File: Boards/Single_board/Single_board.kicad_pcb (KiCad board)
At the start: 2 copper layers, 169.9 x 190.9 mm, 116 parts, among them J1 POWER, J2 ICSP, J3 918-468K2029E50001, J4 918-468K2029E50001, J5 918-468K2029E50001, SW1 2V~12V SMD Mechanical Keyboar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, SW10 2V~12V SMD Mechanical Keyboar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, SW11 2V~12V SMD Mechanical Keyboar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, SW12 2V~12V SMD Mechanical Keyboar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, SW13 2V~12V SMD Mechanical Keyboar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, SW14 2V~12V SMD Mechanical Keyboar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, SW15 2V~12V SMD Mechanical Keyboar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, SW16 2V~12V SMD Mechanical Keyboar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, SW17 2V~12V SMD Mechanical Keyboar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, SW18 2V~12V SMD Mechanical Keyboar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, SW19 2V~12V SMD Mechanical Keyboar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, SW2 2V~12V SMD Mechanical Keyboar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, SW3 2V~12V SMD Mechanical Keyboar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, SW4 2V~12V SMD Mechanical Keyboar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, SW5 2V~12V SMD Mechanical Keyboar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, SW6 2V~12V SMD Mechanical Keyboar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, SW7 2V~12V SMD Mechanical Keyboar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, SW8 2V~12V SMD Mechanical Keyboar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, SW9 2V~12V SMD Mechanical Keyboar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, U2 ATmega328P-A, U3 CH340C

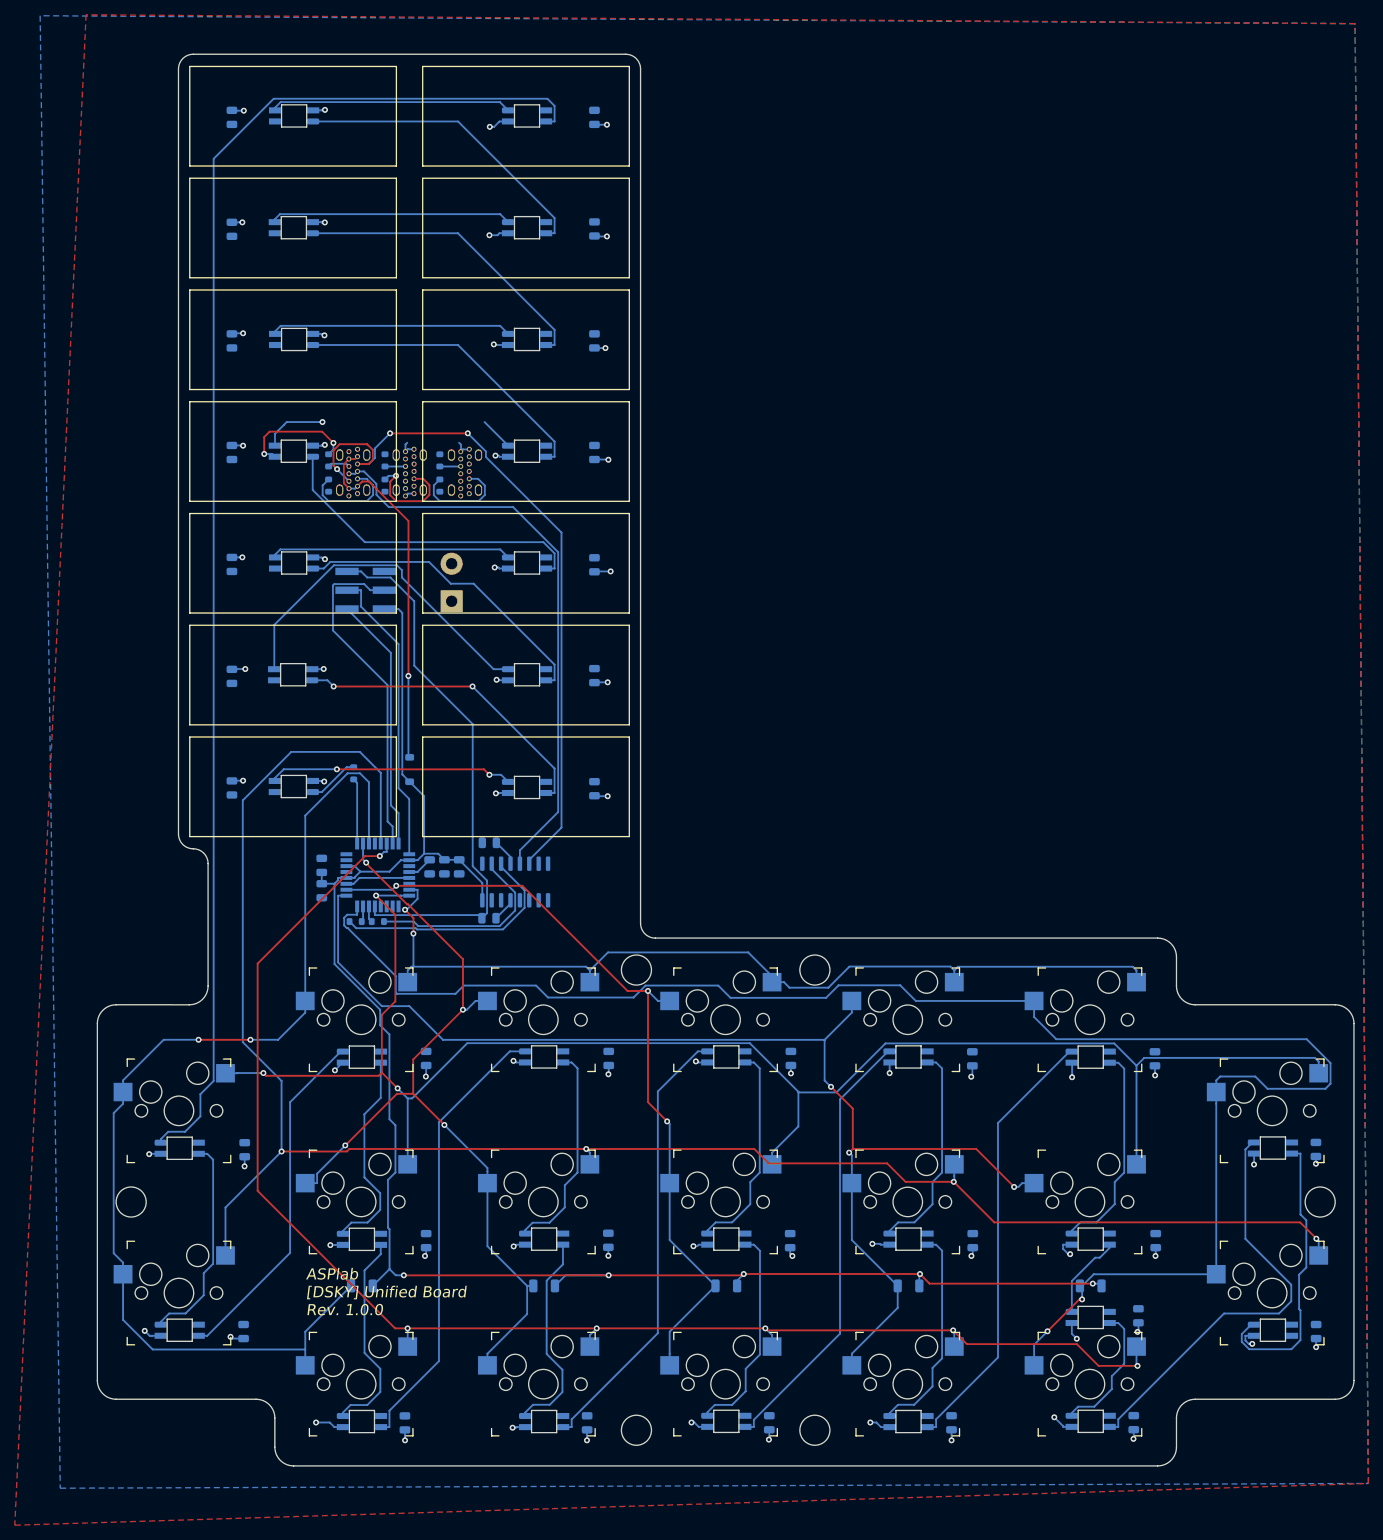
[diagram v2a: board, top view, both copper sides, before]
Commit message: Autoroute and change rgb led footprint
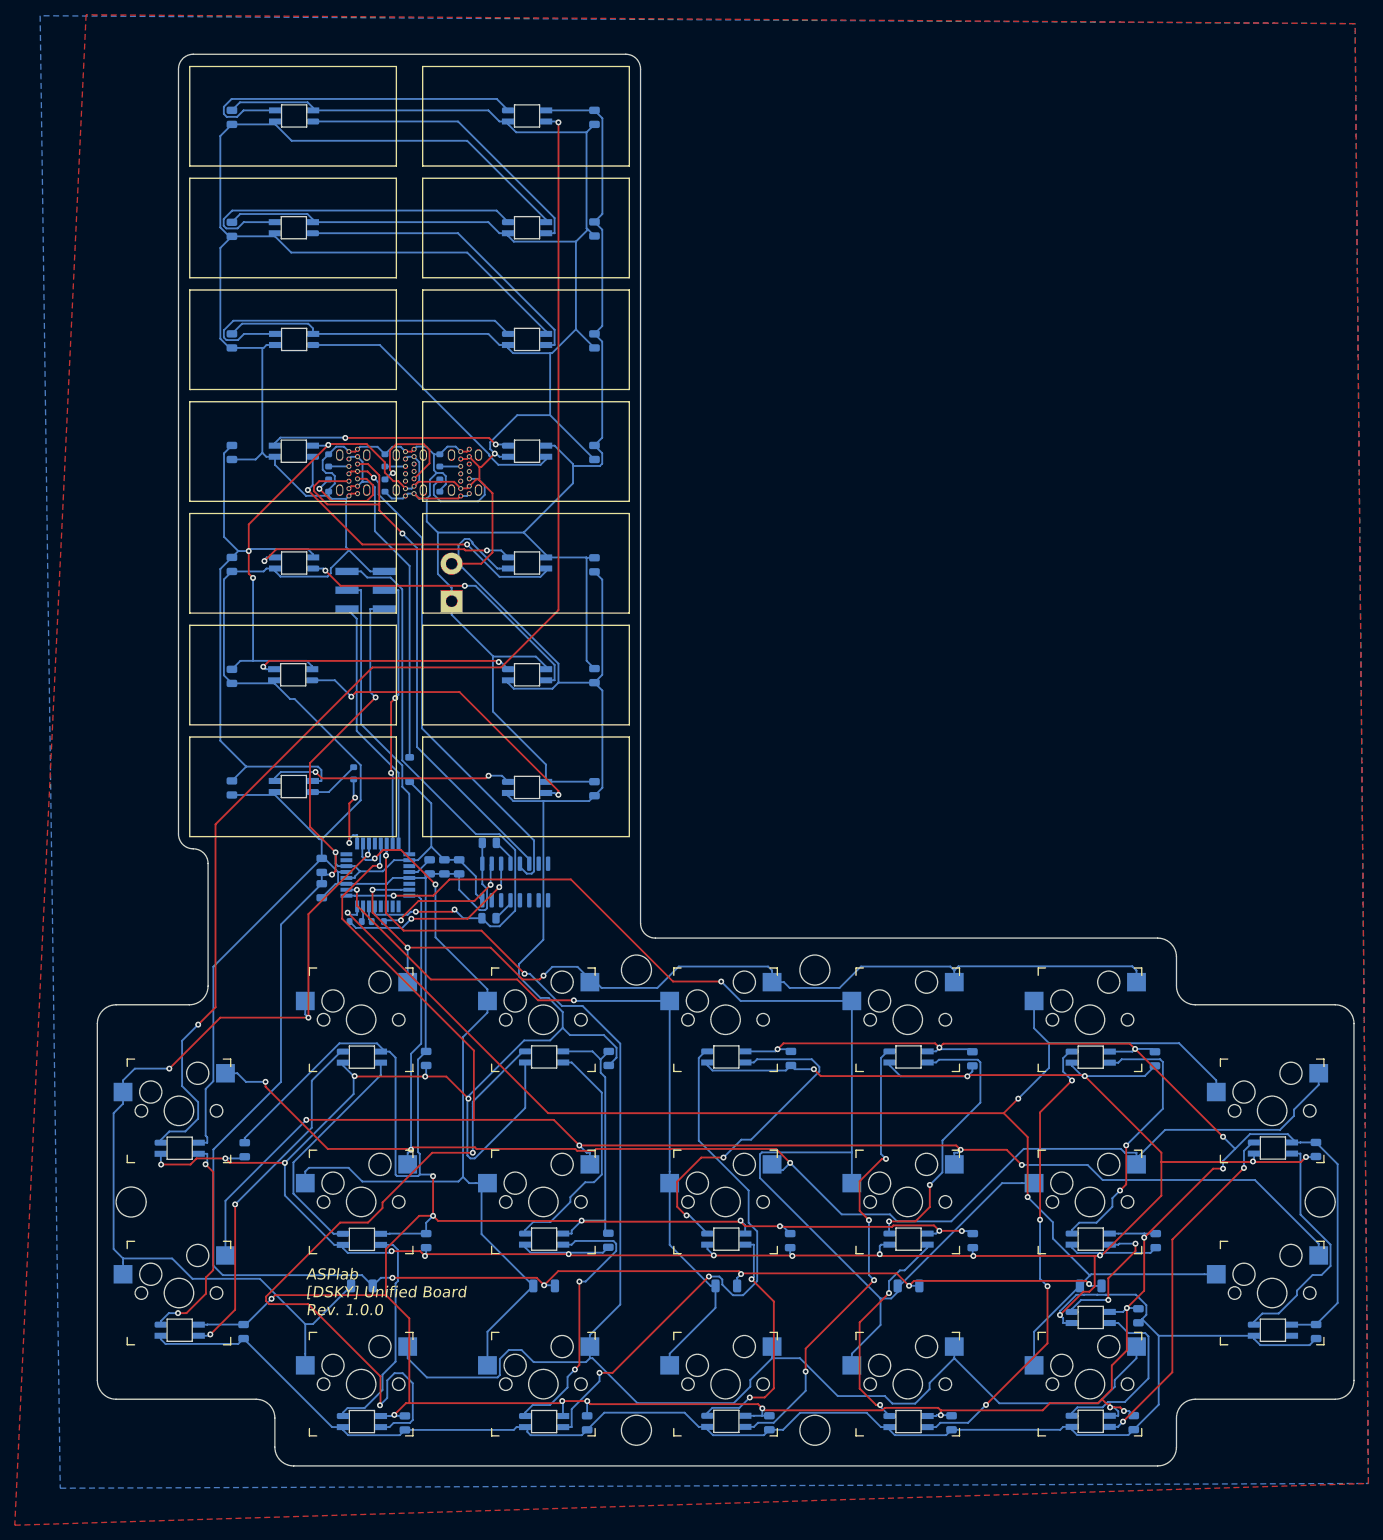
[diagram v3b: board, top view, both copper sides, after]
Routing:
- net GND: track 31.2 -> 1175.9 mm, vias 2 -> 22
- net 5V10A: track 119.2 -> 1129.4 mm, vias 68 -> 24
- net 5V1A: track 235.8 -> 273.0 mm, vias 5 -> 8
- net Net-(D19-DOUT): track 60.8 -> 95.4 mm, vias 0 -> 2
- net Y2: track 251.1 -> 221.7 mm, vias 4 -> 5
- net X4: track 229.8 -> 206.5 mm, vias 2 -> 3
- net Y3: track 197.5 -> 219.0 mm, vias 6 -> 2
- net X0: track 147.9 -> 127.4 mm, vias 2 -> 3
- net Net-(D7-DOUT): track 13.2 -> 32.7 mm, vias 1 -> 2
- net Net-(U3-UD-): track 97.3 -> 79.7 mm, vias 3 -> 1
- net Net-(D23-DOUT): track 28.9 -> 45.6 mm, vias 0 -> 2
- net Net-(D10-DIN): track 32.6 -> 48.1 mm
- net Net-(D13-DOUT): track 32.7 -> 48.0 mm
- net Net-(D11-DOUT): track 32.7 -> 47.9 mm
- net Net-(D14-DOUT): track 190.5 -> 175.3 mm, vias 0 -> 2
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- added copper zone on B.Cu, net 5V10A
- added copper zone on F.Cu, net GND
- removed copper zone on F.Cu, net 5V10A
- removed copper zone on B.Cu, net GND

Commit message: Fix led footprint & autoroute
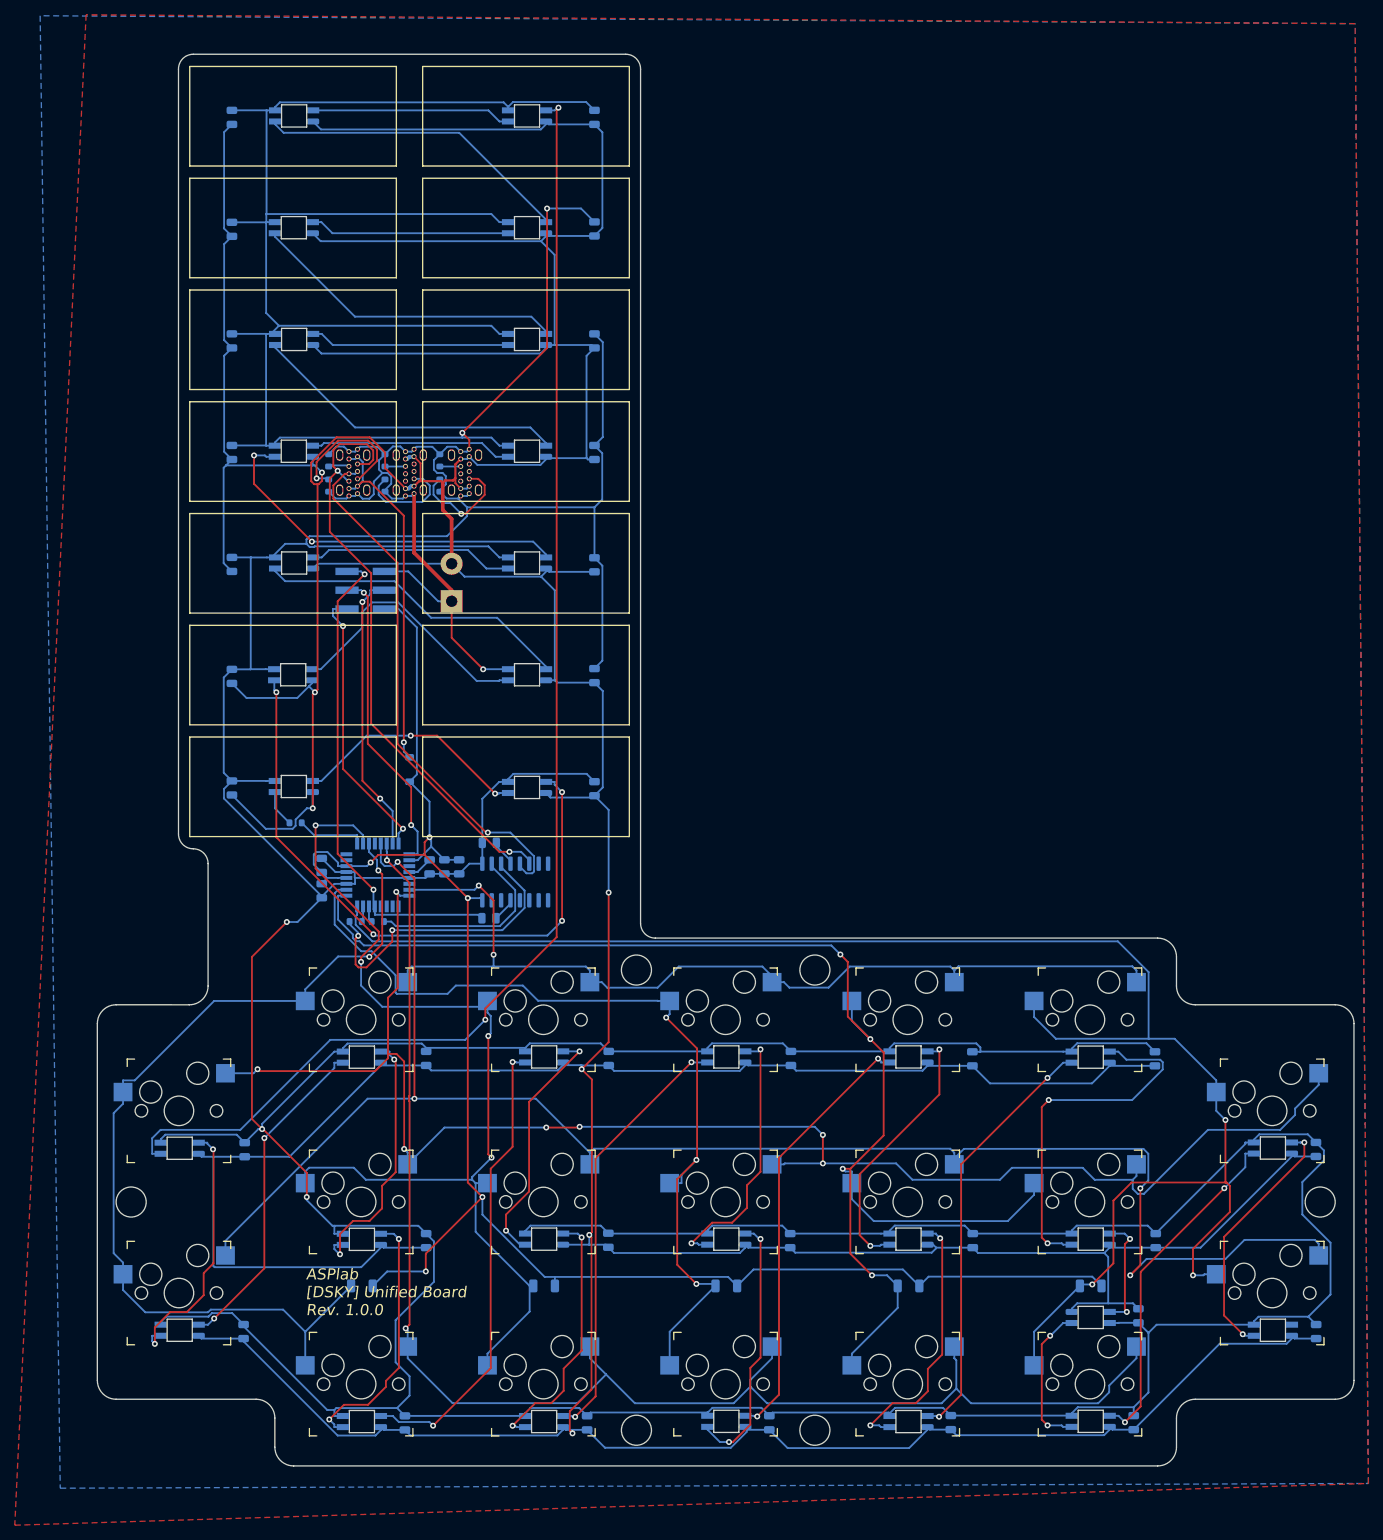
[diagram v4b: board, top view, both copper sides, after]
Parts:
- moved R1 10.3 mm to (149.5, 139.7), turned to 180 degrees
- moved C35 0.10 mm to (238.1, 220.8)
- turned C10 to -90 degrees
- turned C12 to -90 degrees
- turned C14 to -90 degrees
- turned C16 to -90 degrees
- turned C18 to -90 degrees
- turned C20 to -90 degrees
- turned C38 to 90 degrees
- turned C8 to -90 degrees
- turned D10 to 0 degrees
- turned D12 to 0 degrees
- turned D14 to 0 degrees
- turned D15 to 0 degrees
- turned D16 to 0 degrees
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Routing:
- net 5V10A: track 1129.4 -> 1053.1 mm, vias 24 -> 7
- net Net-(D2-DOUT): track 42.4 -> 86.7 mm, vias 2 -> 4
- net 5V1A: track 273.0 -> 239.0 mm, vias 8 -> 5
- net Net-(D19-DOUT): track 95.4 -> 63.0 mm
- net X4: track 206.5 -> 228.0 mm
- net Net-(D10-DIN): track 48.1 -> 27.0 mm
- net Net-(D13-DOUT): track 48.0 -> 27.0 mm
- net Net-(D11-DOUT): track 47.9 -> 27.1 mm
- net X1: track 116.1 -> 136.1 mm, vias 2 -> 4
- net Y3: track 219.0 -> 200.8 mm
- net X2: track 106.0 -> 121.9 mm, vias 2 -> 3
- net Net-(D22-DOUT): track 74.0 -> 58.3 mm
- net RESET: track 82.3 -> 67.4 mm
- net Net-(U3-RXD): track 26.2 -> 41.0 mm
- net Net-(D29-DOUT): track 37.2 -> 49.3 mm
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
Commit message: Some stitching but led arrangement is suboptimal
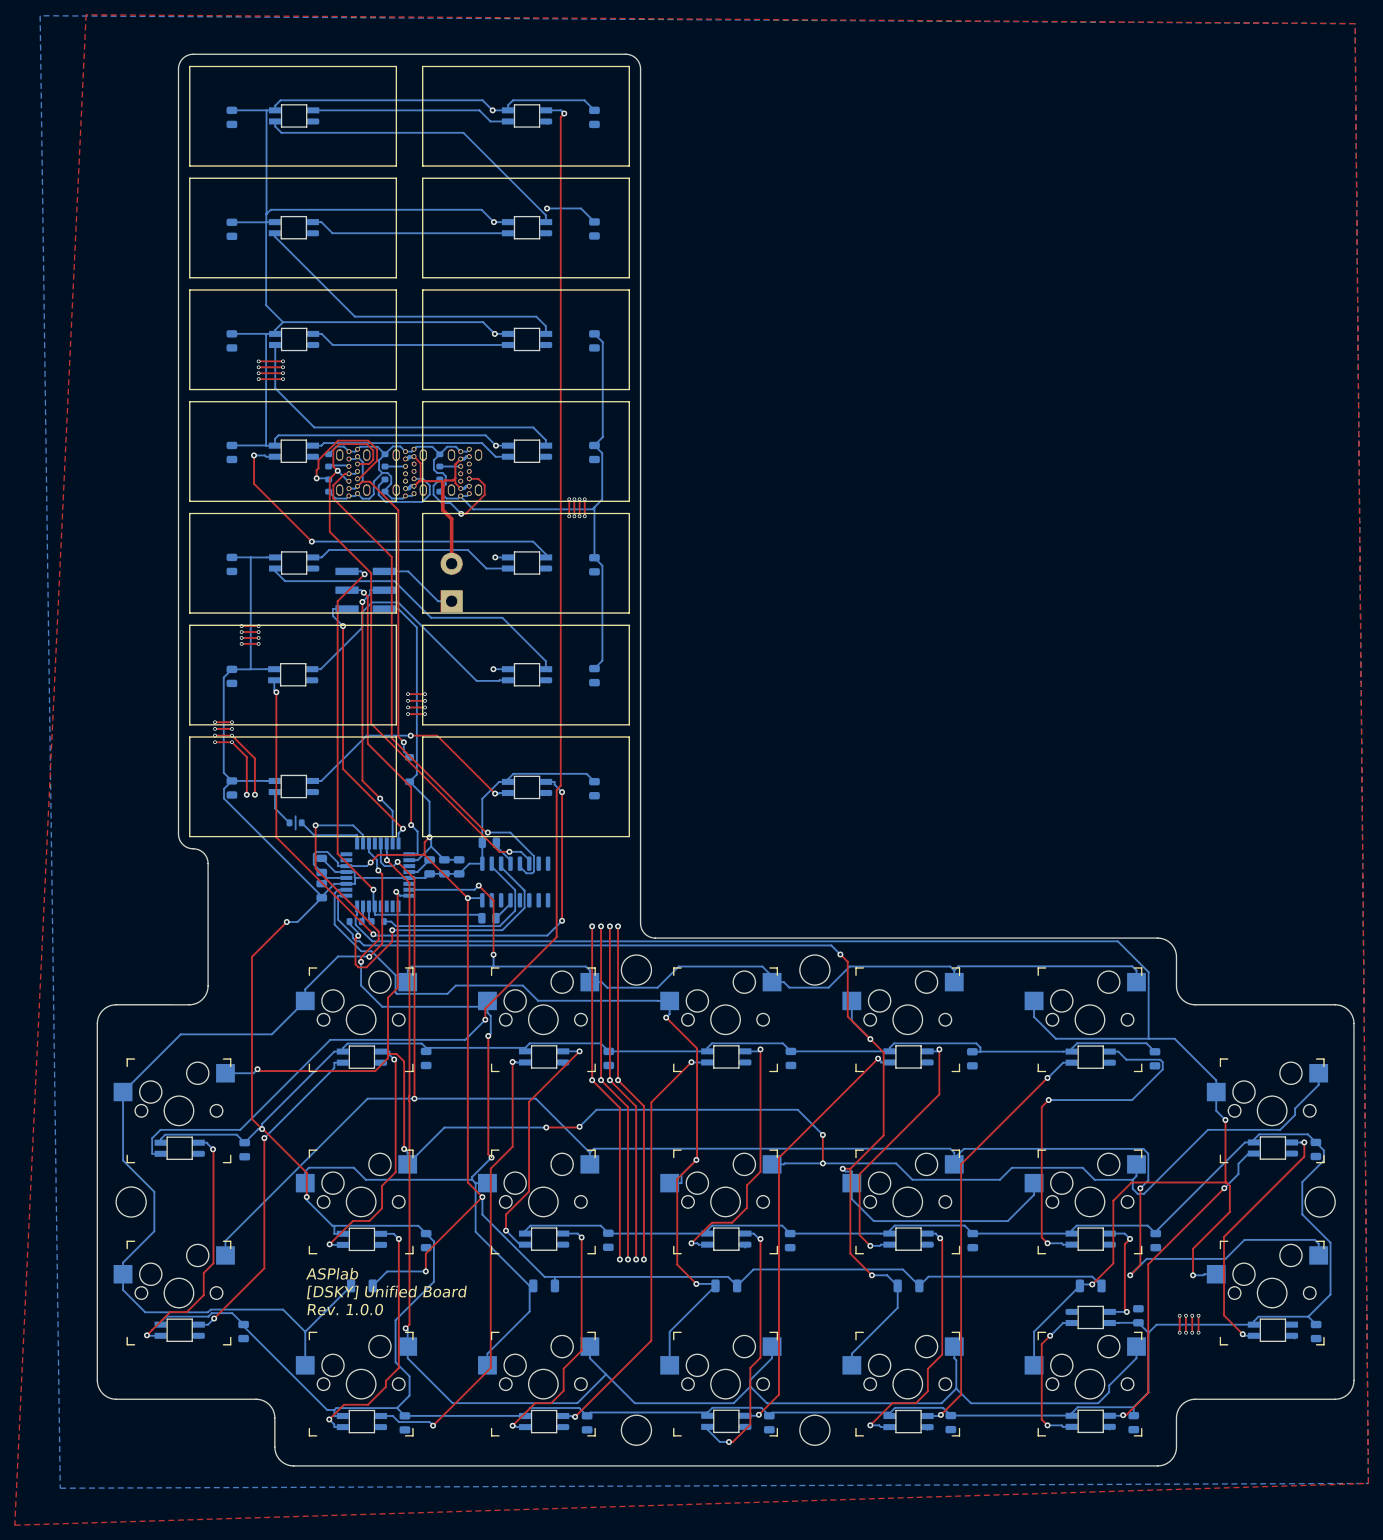
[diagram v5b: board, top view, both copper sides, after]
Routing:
- net 5V10A: track 1053.1 -> 301.8 mm, vias 7 -> 62
- net GND: track 1186.1 -> 1064.2 mm, vias 6 -> 10
- net Net-(D8-DOUT): track 42.7 -> 46.1 mm
- net Y1: track 215.6 -> 217.5 mm
- net Net-(D17-DOUT): track 36.1 -> 34.4 mm
- net X0: track 128.0 -> 129.5 mm
- net Net-(D32-DOUT): track 46.7 -> 45.2 mm
- net Net-(D15-DOUT): track 35.8 -> 34.5 mm
- net Net-(D12-DOUT): track 42.7 -> 43.2 mm

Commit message: Optimize led positions
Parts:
- D1, D10, D11, D12, D13, D14, D15, D16, D17, D18, D19, D2, D20, D21, D22, D23, D24, D25, D26, D27, D28, D29, D3, D30, D31, D32, D33, D34, D4, D5, D6, D7, D8, D9: footprint Project Libraries:SK6812-MINI-E -> Project Libraries:SK6812-MINI-E_Clearance
- moved D14 90.8 mm to (180.8, 134.9)
- moved C21 90.8 mm to (189.9, 135.1)
- moved C20 90.0 mm to (189.9, 119.8)
- moved D13 81.9 mm to (180.8, 119.6)
- moved C13 66.8 mm to (140.9, 59.4)
- moved C11 57.6 mm to (140.9, 89.6)
- moved C18 57.6 mm to (189.9, 89.6)
- moved D6 55.2 mm to (149.3, 59.2)
- moved C9 51.3 mm to (140.9, 119.9)
- moved C16 51.3 mm to (189.9, 59.4)
- moved D15 50.8 mm to (183.1, 171.3)
- moved C22 50.7 mm to (191.9, 171.5)
- moved C30 49.4 mm to (213.6, 220.8)
- moved C32 49.4 mm to (216.5, 171.5)
- moved C36 49.3 mm to (262.9, 220.8)
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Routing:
- net GND: track 1064.2 -> 0.00 mm, vias 10 -> 0
- net 5V10A: track 301.8 -> 0.00 mm, vias 62 -> 0
- net 5V1A: track 239.0 -> 0.00 mm, vias 5 -> 0
- net X4: track 228.0 -> 0.00 mm, vias 3 -> 0
- net Y2: track 227.1 -> 0.00 mm, vias 4 -> 0
- net Y1: track 217.5 -> 0.00 mm, vias 7 -> 0
- net Y3: track 200.8 -> 0.00 mm, vias 2 -> 0
- net Net-(D14-DOUT): track 184.6 -> 0.00 mm, vias 2 -> 0
- net X3: track 182.1 -> 0.00 mm, vias 4 -> 0
- net X1: track 136.1 -> 0.00 mm, vias 4 -> 0
- net Y0: track 132.1 -> 0.00 mm, vias 2 -> 0
- net X0: track 129.5 -> 0.00 mm, vias 2 -> 0
- net X2: track 121.9 -> 0.00 mm, vias 3 -> 0
- net Net-(D2-DOUT): track 86.7 -> 0.00 mm, vias 4 -> 0
- net Net-(U3-UD-): track 81.3 -> 0.00 mm, vias 2 -> 0
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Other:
- board text added: "5V"
- board text added: "Display"
- board text added: "GND"
- board text added: "ICSP"
- board text added: "OrangePi Power"
- board text added: "Serial"
- board text removed: "Rev. 1.0.0"
